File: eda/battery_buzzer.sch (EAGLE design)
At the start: 25 parts, among them Q2 IRFML8244, U1 ISL83491SOIC, U2 ATTINY1634

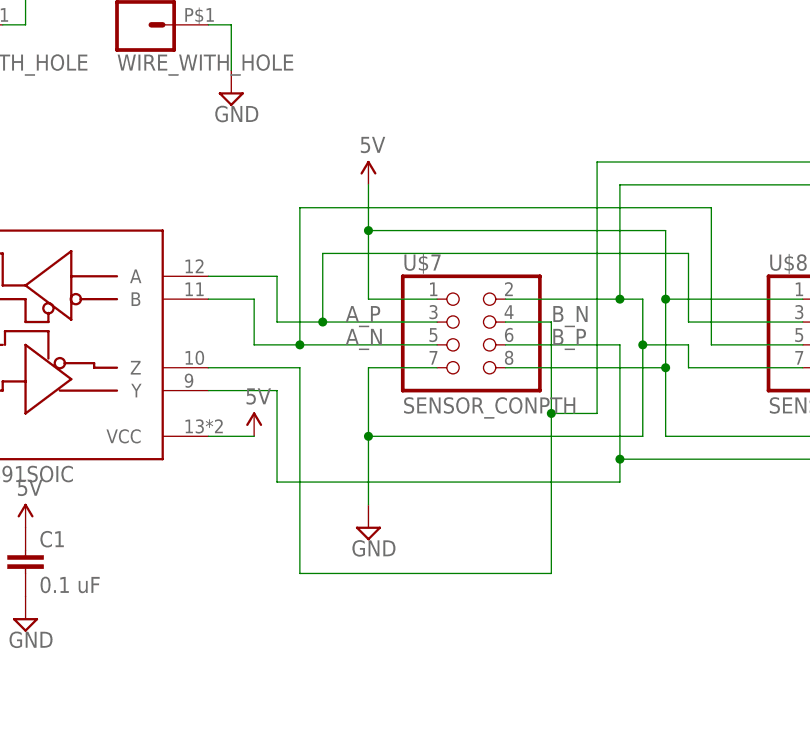
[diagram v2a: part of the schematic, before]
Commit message: Update all smart-sensor protocol boards to use new pinout
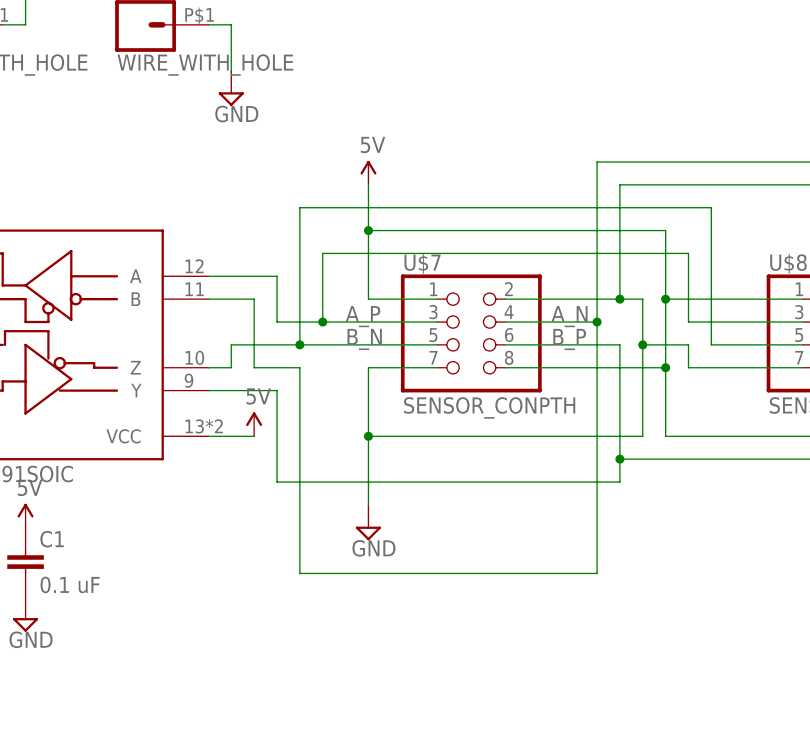
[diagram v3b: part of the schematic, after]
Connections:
- net A_N: now also U$7.4, U$8.4; no longer U$7.5, U$8.5
- net B_N: now also U$7.5, U$8.5; no longer U$7.4, U$8.4
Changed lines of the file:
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@@
 </segment>
 </net>
-<net name="A_N" class="0">
+<net name="B_N" class="0">
 <segment>
 <pinref part="U$7" gate="G$1" pin="5"/>
 <wire x1="190.5" y1="137.16" x2="175.26" y2="137.16" width="0.1524" layer="91"/>
-<wire x1="175.26" y1="137.16" x2="170.18" y2="137.16" width="0.1524" layer="91"/>
-<wire x1="170.18" y1="137.16" x2="170.18" y2="142.24" width="0.1524" layer="91"/>
-<pinref part="U1" gate="G$1" pin="B"/>
-<wire x1="170.18" y1="142.24" x2="165.1" y2="142.24" width="0.1524" layer="91"/>
 <label x="180.34" y="137.16" size="1.778" layer="95"/>
 <pinref part="U$8" gate="G$1" pin="5"/>
@@
 <wire x1="175.26" y1="152.4" x2="175.26" y2="137.16" width="0.1524" layer="91"/>
 <junction x="175.26" y="137.16"/>
+<pinref part="U1" gate="G$1" pin="Z"/>
+<wire x1="175.26" y1="137.16" x2="167.64" y2="137.16" width="0.1524" layer="91"/>
+<wire x1="167.64" y1="137.16" x2="167.64" y2="134.62" width="0.1524" layer="91"/>
+<wire x1="167.64" y1="134.62" x2="165.1" y2="134.62" width="0.1524" layer="91"/>
 </segment>
 </net>
-<net name="B_N" class="0">
+<net name="A_N" class="0">
 <segment>
 <pinref part="U$7" gate="G$1" pin="4"/>
-<wire x1="198.12" y1="139.7" x2="203.2" y2="139.7" width="0.1524" layer="91"/>
-<wire x1="203.2" y1="139.7" x2="203.2" y2="129.54" width="0.1524" layer="91"/>
-<wire x1="203.2" y1="129.54" x2="203.2" y2="111.76" width="0.1524" layer="91"/>
-<wire x1="203.2" y1="111.76" x2="175.26" y2="111.76" width="0.1524" layer="91"/>
+<wire x1="198.12" y1="139.7" x2="208.28" y2="139.7" width="0.1524" layer="91"/>
+<wire x1="208.28" y1="139.7" x2="208.28" y2="111.76" width="0.1524" layer="91"/>
+<wire x1="208.28" y1="111.76" x2="175.26" y2="111.76" width="0.1524" layer="91"/>
 <wire x1="175.26" y1="111.76" x2="175.26" y2="134.62" width="0.1524" layer="91"/>
-<pinref part="U1" gate="G$1" pin="Z"/>
-<wire x1="175.26" y1="134.62" x2="165.1" y2="134.62" width="0.1524" layer="91"/>
 <label x="203.2" y="139.7" size="1.778" layer="95"/>
 <pinref part="U$8" gate="G$1" pin="4"/>
@@
 <wire x1="246.38" y1="139.7" x2="246.38" y2="157.48" width="0.1524" layer="91"/>
 <wire x1="246.38" y1="157.48" x2="208.28" y2="157.48" width="0.1524" layer="91"/>
-<wire x1="208.28" y1="157.48" x2="208.28" y2="129.54" width="0.1524" layer="91"/>
-<wire x1="208.28" y1="129.54" x2="203.2" y2="129.54" width="0.1524" layer="91"/>
-<junction x="203.2" y="129.54"/>
+<wire x1="208.28" y1="157.48" x2="208.28" y2="139.7" width="0.1524" layer="91"/>
+<pinref part="U1" gate="G$1" pin="B"/>
+<wire x1="165.1" y1="142.24" x2="170.18" y2="142.24" width="0.1524" layer="91"/>
+<wire x1="170.18" y1="142.24" x2="170.18" y2="134.62" width="0.1524" layer="91"/>
+<wire x1="170.18" y1="134.62" x2="175.26" y2="134.62" width="0.1524" layer="91"/>
+<junction x="208.28" y="139.7"/>
 </segment>
 </net>
